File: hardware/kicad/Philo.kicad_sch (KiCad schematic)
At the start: 0 parts

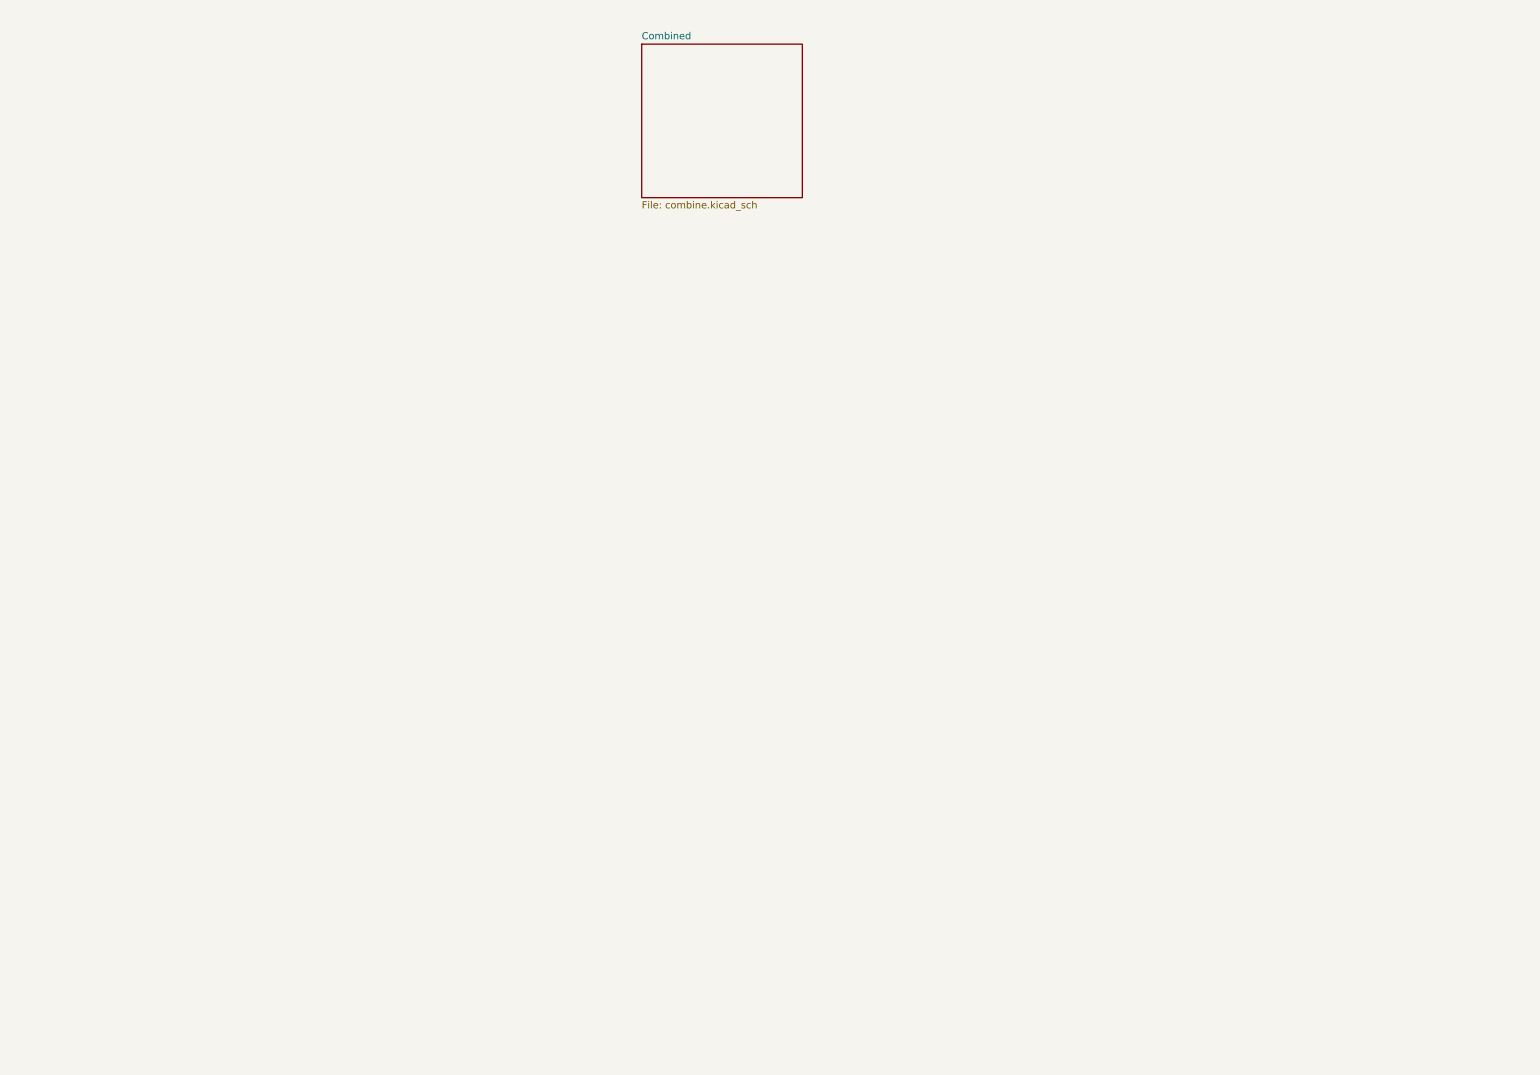
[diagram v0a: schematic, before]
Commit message: Fix U1 ref designator in schematic — sync with PCB
Changed GY-521 8-pin header from J15 → U1 to match PCB.
Symbol was re-annotated when MPU-6050 was replaced with
Connector_Generic:Conn_01x08 during crash recovery session.

Co-Authored-By: Claude Sonnet 4.6 <noreply@anthropic.com>
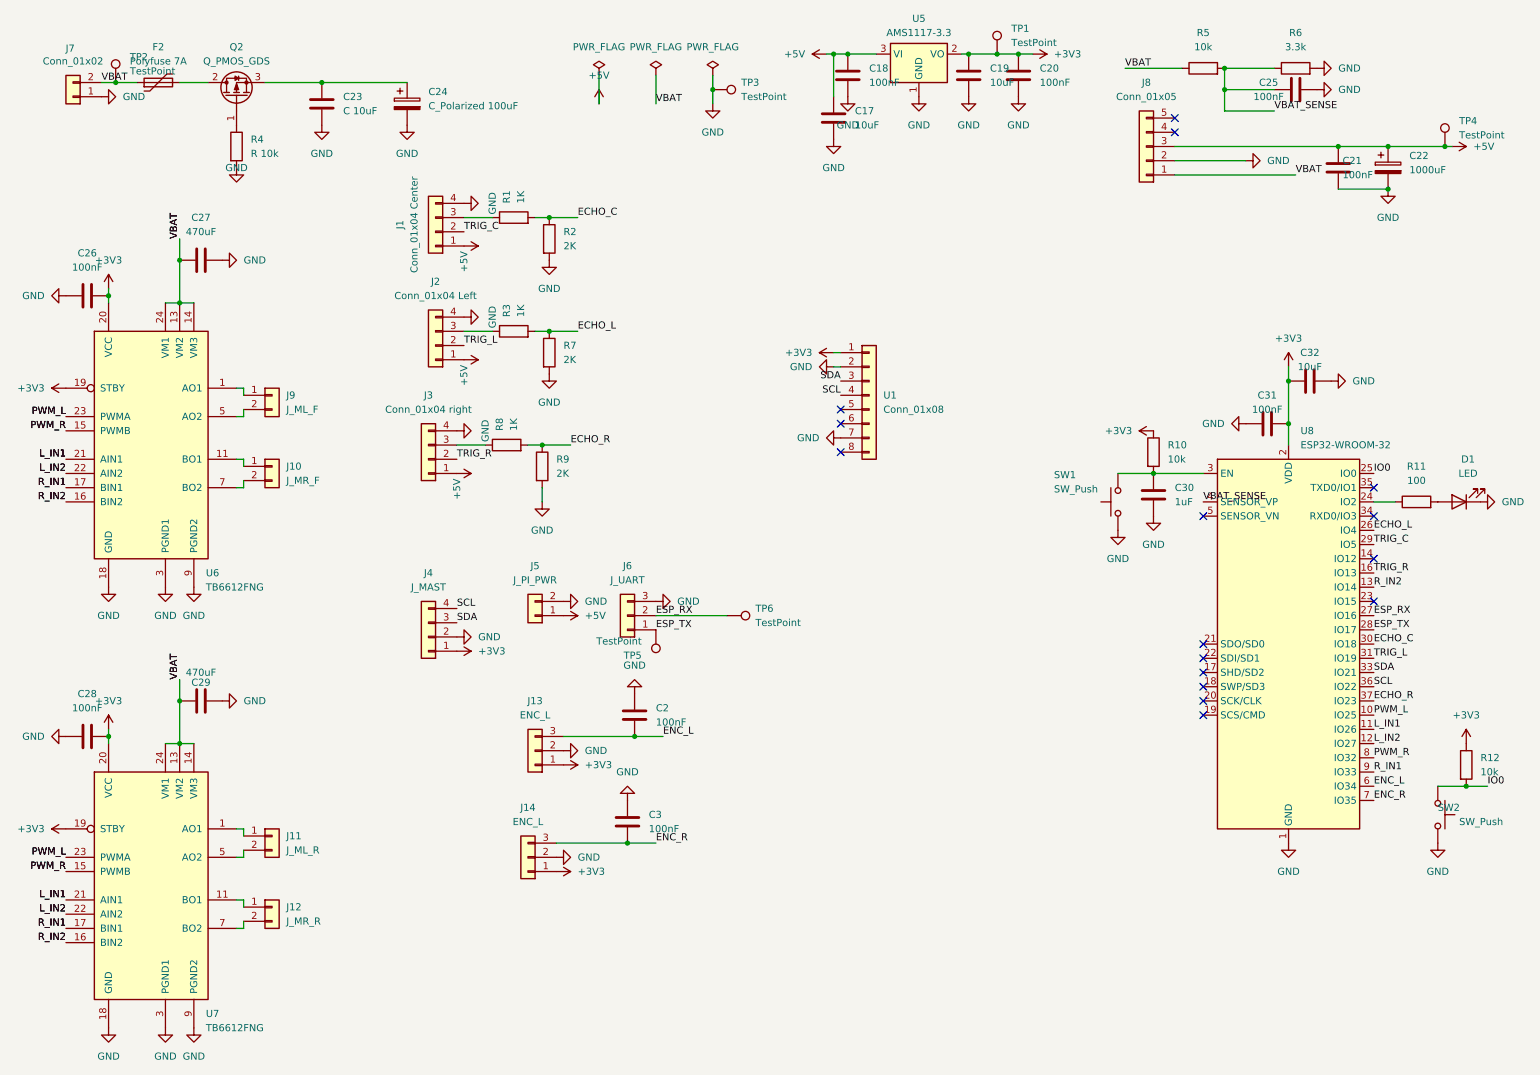
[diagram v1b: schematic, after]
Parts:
- added C17, C19, C32: 10uF, Capacitor_SMD:C_0805_2012Metric, symbol Device:C
- added C18, C2, C20, C21, C25, C26, C28, C3, C31: 100nF, Capacitor_SMD:C_0603_1608Metric, symbol Device:C
- added C22: 1000uF, Capacitor_THT:CP_Radial_D12.5mm_P5.00mm, symbol Device:C_Polarized
- added C23: C 10uF, Capacitor_SMD:C_0805_2012Metric, symbol Device:C
- added C24: C_Polarized 100uF, Capacitor_THT:CP_Radial_D6.3mm_P2.50mm, symbol Device:C_Polarized
- added C27, C29: 470uF, Capacitor_THT:CP_Radial_D10.0mm_P5.00mm, symbol Device:C
- added C30: 1uF, Capacitor_SMD:C_0603_1608Metric, symbol Device:C
- added D1: LED, LED_SMD:LED_0805_2012Metric, symbol Device:LED
- added F2: Polyfuse 7A, Capacitor_THT:CP_Radial_D10.0mm_P5.00mm, symbol Device:Polyfuse
- added J1: Conn_01x04 Center, Connector_PinHeader_2.54mm:PinHeader_1x04_P2.54mm_Vertical, symbol Connector_Generic:Conn_01x04
- added J10: J_MR_F, Connector_PinHeader_2.54mm:PinHeader_1x02_P2.54mm_Vertical, symbol Connector_Generic:Conn_01x02
- added J11: J_ML_R, Connector_PinHeader_2.54mm:PinHeader_1x02_P2.54mm_Vertical, symbol Connector_Generic:Conn_01x02
- added J12: J_MR_R, Connector_PinHeader_2.54mm:PinHeader_1x02_P2.54mm_Vertical, symbol Connector_Generic:Conn_01x02
- added J13, J14: ENC_L, Connector_PinHeader_2.54mm:PinHeader_1x03_P2.54mm_Vertical, symbol Connector_Generic:Conn_01x03
- added J2: Conn_01x04 Left, Connector_PinHeader_2.54mm:PinHeader_1x04_P2.54mm_Vertical, symbol Connector_Generic:Conn_01x04
- added J3: Conn_01x04 right, Connector_PinHeader_2.54mm:PinHeader_1x04_P2.54mm_Vertical, symbol Connector_Generic:Conn_01x04
- added J4: J_MAST, Connector_PinHeader_2.54mm:PinHeader_1x04_P2.54mm_Vertical, symbol Connector_Generic:Conn_01x04
- added J5: J_PI_PWR, Connector_PinHeader_2.54mm:PinHeader_1x02_P2.54mm_Vertical, symbol Connector_Generic:Conn_01x02
- added J6: J_UART, Connector_PinHeader_2.54mm:PinHeader_1x03_P2.54mm_Vertical, symbol Connector_Generic:Conn_01x03
- added J7: Conn_01x02, Connector_PinHeader_2.54mm:PinHeader_1x02_P2.54mm_Vertical, symbol Connector_Generic:Conn_01x02
- added J8: Conn_01x05, Connector_PinHeader_2.54mm:PinHeader_1x05_P2.54mm_Vertical, symbol Connector_Generic:Conn_01x05
- added J9: J_ML_F, Connector_PinHeader_2.54mm:PinHeader_1x02_P2.54mm_Vertical, symbol Connector_Generic:Conn_01x02
- added Q2: Q_PMOS_GDS, Package_TO_SOT_SMD:TO-252-3_TabPin2, symbol Transistor_FET:Q_PMOS_GDS
- added R1, R3, R8: 1K, Resistor_SMD:R_0603_1608Metric, symbol Device:R
- added R10, R12, R5: 10k, Resistor_SMD:R_0603_1608Metric, symbol Device:R
- added R11: 100, Resistor_SMD:R_0603_1608Metric, symbol Device:R
- added R2, R7, R9: 2K, Resistor_SMD:R_0603_1608Metric, symbol Device:R
- added R4: R 10k, Resistor_SMD:R_0603_1608Metric, symbol Device:R
- added R6: 3.3k, Resistor_SMD:R_0603_1608Metric, symbol Device:R
- added SW1, SW2: SW_Push, Button_Switch_THT:SW_PUSH_6mm, symbol Switch:SW_Push
- added TP1, TP2, TP3, TP4, TP5, TP6: TestPoint, TestPoint:TestPoint_Pad_D1.5mm, symbol Connector:TestPoint
- added U1: Conn_01x08, symbol Connector_Generic:Conn_01x08
- added U5: AMS1117-3.3, Package_TO_SOT_SMD:SOT-223-3_TabPin2, symbol Regulator_Linear:AMS1117-3.3
- added U6, U7: TB6612FNG, Package_SO:SSOP-24_5.3x8.2mm_P0.65mm, symbol Driver_Motor:TB6612FNG
- added U8: ESP32-WROOM-32, RF_Module:ESP32-WROOM-32, symbol RF_Module:ESP32-WROOM-32
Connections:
- new net: J3.3 (Pin_3), R8.1
- new net: J1.3 (Pin_3), R1.1
- new net: J9.1 (Pin_1), U6.1 (AO1), U6.2 (AO1)
- new net: J9.2 (Pin_2), U6.5 (AO2), U6.6 (AO2)
- new net: Q2.1 (G), R4.1
- new net: J2.3 (Pin_3), R3.1
- new net: J11.1 (Pin_1), U7.1 (AO1), U7.2 (AO1)
- new net: J12.1 (Pin_1), U7.11 (BO1), U7.12 (BO1)
- new net: J11.2 (Pin_2), U7.5 (AO2), U7.6 (AO2)
- new net: J12.2 (Pin_2), U7.7 (BO2), U7.8 (BO2)
- new net: J10.1 (Pin_1), U6.11 (BO1), U6.12 (BO1)
- new net: J10.2 (Pin_2), U6.7 (BO2), U6.8 (BO2)
- new net: C30.1, R10.2, SW1.2, U8.3 (EN)
- new net: R11.1, U8.24 (IO2)
- new net: D1.2 (A), R11.2
- new net: C23.1, C24.1, Q2.3 (S)
- new net: F2.2, Q2.2 (D)
- new net +3V3: C19.1, C20.1, C26.2, C28.2, C31.1, C32.1, J13.1 (Pin_1), J14.1 (Pin_1), J4.1 (Pin_1), R10.1, R12.1, TP1.1, U1.1 (Pin_1), U5.2 (VO), U6.19 (STBY), U6.20 (VCC), U7.19 (STBY), U7.20 (VCC), U8.2 (VDD)
- new net +5V: C17.1, C18.1, C21.1, C22.1, J1.1 (Pin_1), J2.1 (Pin_1), J3.1 (Pin_1), J5.1 (Pin_1), J8.3 (Pin_3), TP4.1, U5.3 (VI)
- new net ECHO_C: R1.2, R2.1, U8.30 (IO18)
- new net ECHO_L: R3.2, R7.1, U8.26 (IO4)
- new net ECHO_R: R8.2, R9.1, U8.37 (IO23)
- new net ENC_L: C2.2, J13.3 (Pin_3), U8.6 (IO34)
- new net ENC_R: C3.2, J14.3 (Pin_3), U8.7 (IO35)
- new net ESP_RX: J6.2 (Pin_2), TP6.1, U8.27 (IO16)
- new net ESP_TX: J6.1 (Pin_1), TP5.1, U8.28 (IO17)
- new net GND: C17.2, C18.2, C19.2, C2.1, C20.2, C21.2, C22.2, C23.2, C24.2, C25.2, C26.1, C27.2, C28.1, C29.2, C3.1, C30.2, C31.2, C32.2, D1.1 (K), J1.4 (Pin_4), J13.2 (Pin_2), J14.2 (Pin_2), J2.4 (Pin_4), J3.4 (Pin_4), J4.2 (Pin_2), J5.2 (Pin_2), J6.3 (Pin_3), J7.1 (Pin_1), J8.2 (Pin_2), R2.2, R4.2, R6.2, R7.2, R9.2, SW1.1, SW2.2, TP3.1, U1.2 (Pin_2), U1.7 (Pin_7), U5.1 (GND), U6.10 (PGND2), U6.18 (GND), U6.3 (PGND1), U6.4 (PGND1), U6.9 (PGND2), U7.10 (PGND2), U7.18 (GND), U7.3 (PGND1), U7.4 (PGND1), U7.9 (PGND2), U8.1 (GND), U8.15 (GND), U8.38 (GND), U8.39 (GND)
- new net IO0: R12.2, SW2.1, U8.25 (IO0)
- new net L_IN1: U6.21 (AIN1), U7.21 (AIN1), U8.11 (IO26)
- new net L_IN2: U6.22 (AIN2), U7.22 (AIN2), U8.12 (IO27)
- new net PWM_L: U6.23 (PWMA), U7.23 (PWMA), U8.10 (IO25)
- new net PWM_R: U6.15 (PWMB), U7.15 (PWMB), U8.8 (IO32)
- new net R_IN1: U6.17 (BIN1), U7.17 (BIN1), U8.9 (IO33)
- new net R_IN2: U6.16 (BIN2), U7.16 (BIN2), U8.13 (IO14)
- new net SCL: J4.4 (Pin_4), U1.4 (Pin_4), U8.36 (IO22)
- new net SDA: J4.3 (Pin_3), U1.3 (Pin_3), U8.33 (IO21)
- new net TRIG_C: J1.2 (Pin_2), U8.29 (IO5)
- new net TRIG_L: J2.2 (Pin_2), U8.31 (IO19)
- new net TRIG_R: J3.2 (Pin_2), U8.16 (IO13)
- new net VBAT: C27.1, C29.1, F2.1, J7.2 (Pin_2), J8.1 (Pin_1), R5.1, TP2.1, U6.13 (VM2), U6.14 (VM3), U6.24 (VM1), U7.13 (VM2), U7.14 (VM3), U7.24 (VM1)
- new net VBAT_SENSE: C25.1, R5.2, R6.1, U8.4 (SENSOR_VP)
- no-connect marks 0 -> 16
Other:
- removed sheet Combined

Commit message: Reorganise repo — all files in proper folders, add gerbers and STEP
- Move PCB files (Philo- main.*) from root → hardware/kicad/
- Move DRC.rpt from root → hardware/kicad/
- Move PRE_BUILD_LOCK.md from root → docs/
- Add 3D STEP export → mechanical/
- Add Gerber/drill files → hardware/kicad/gerbers/
- Add schematic project settings files (Philo- schematic.kicad_pro/prl)
- Update .gitignore: cover autosave files, borh/ working folder, OS junk
- Fix platformio.ini: pin to espressif32@6.9.0 (fixes pins_arduino.h build error)
- Fix motors.cpp: use Arduino 2.x LEDC API (ledcSetup/ledcAttachPin/ledcWrite)
- Update README: correct folder tree, mark schematic/PCB/firmware as done

Co-Authored-By: Claude Sonnet 4.6 <noreply@anthropic.com>
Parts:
- U1: value Conn_01x08 -> MPU-6050
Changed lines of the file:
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@@
 			)
 		)
-		(property "Value" "Conn_01x08"
+		(property "Value" "MPU-6050"
 			(at 167.64 81.2799 0)
 			(effects
@@
 			(project ""
 				(path "/e6b75d5f-82b0-4e13-a2ef-a855a91f600e"
-					(reference "J15")
+					(reference "U1")
 					(unit 1)
 				)
